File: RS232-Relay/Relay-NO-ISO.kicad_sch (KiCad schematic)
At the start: 7 parts, among them K13 G5V-1, Q13 2N3904

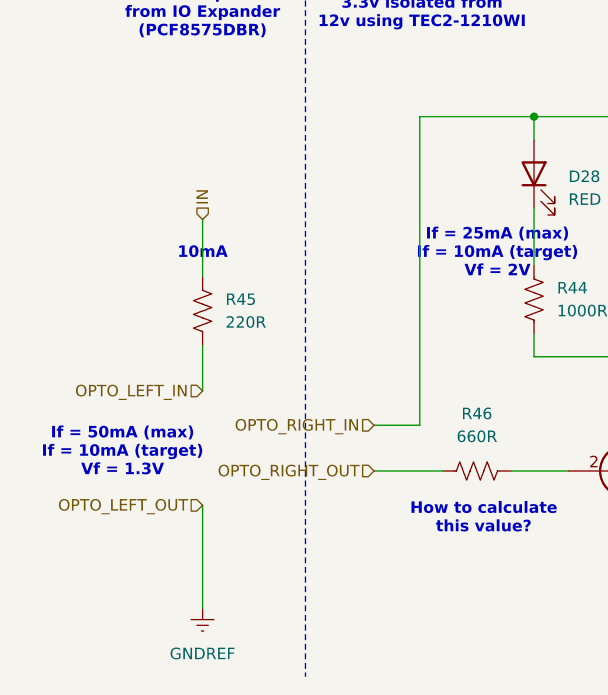
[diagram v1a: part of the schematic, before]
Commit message: Switching to drain rather than source
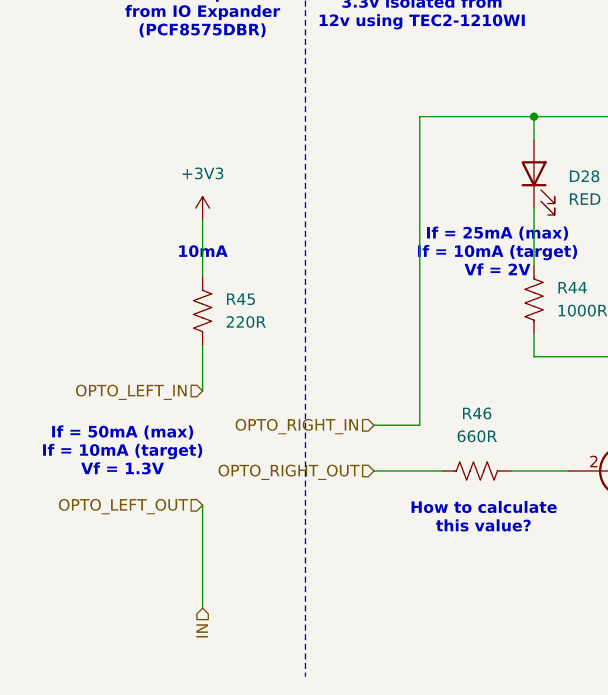
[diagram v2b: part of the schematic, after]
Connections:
- net IN: no longer R45.2
- new net +3V3: R45.2
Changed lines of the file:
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@@
-		)
-	)
-	(hierarchical_label "IN"
-		(shape input)
-		(at 91.44 72.39 90)
-		(fields_autoplaced yes)
-		(effects
-			(font
-				(size 1.27 1.27)
-			)
-			(justify left)
 		)
 	)
@@
 		)
 	)
+	(hierarchical_label "IN"
+		(shape input)
+		(at 91.44 115.57 270)
+		(fields_autoplaced yes)
+		(effects
+			(font
+				(size 1.27 1.27)
+			)
+			(justify right)
+		)
+	)
 	(symbol
-		(lib_id "power:GNDREF")
-		(at 91.44 115.57 0)
+		(lib_id "power:+3V3")
+		(at 91.44 72.39 0)
 		(unit 1)
 		(exclude_from_sim no)
@@
 		(dnp no)
 		(fields_autoplaced yes)
-		(property "Reference" "#PWR069"
-			(at 91.44 121.92 0)
+		(property "Reference" "#PWR052"
+			(at 91.44 76.2 0)
 			(effects
 				(font
@@
 			)
 		)
-		(property "Value" "GNDREF"
-			(at 91.44 120.65 0)
+		(property "Value" "+3V3"
+			(at 91.44 67.31 0)
 			(effects
 				(font
@@
 		)
 		(property "Footprint" ""
-			(at 91.44 115.57 0)
+			(at 91.44 72.39 0)
 			(effects
 				(font
@@
 		)
 		(property "Datasheet" ""
-			(at 91.44 115.57 0)
+			(at 91.44 72.39 0)
 			(effects
 				(font
@@
 			)
 		)
-		(property "Description" "Power symbol creates a global label with name \"GNDREF\" , reference supply ground"
-			(at 91.44 115.57 0)
+		(property "Description" "Power symbol creates a global label with name \"+3V3\""
+			(at 91.44 72.39 0)
 			(effects
 				(font
@@
 		(instances
 			(project "RS232-Relay"
+				(path "/6e416d74-c18a-4d9a-a47c-4314aa8f470f/6243990a-47f3-4383-9005-5094cba86ad2/ed71aacf-ab14-4c62-832c-243c3f9cdc45"
+					(reference "#PWR052")
+					(unit 1)
+				)
 				(path "/6e416d74-c18a-4d9a-a47c-4314aa8f470f/6243990a-47f3-4383-9005-5094cba86ad2/f12f86a4-1d04-4329-8ad3-ff7853ea8b11"
-					(reference "#PWR069")
+					(reference "#PWR02")
 					(unit 1)
 				)
 				(path "/6e416d74-c18a-4d9a-a47c-4314aa8f470f/4cc60208-aa63-44fd-9447-92e9d40fbb60/f12f86a4-1d04-4329-8ad3-ff7853ea8b11"
-					(reference "#PWR072")
+					(reference "#PWR028")
 					(unit 1)
 				)
 				(path "/6e416d74-c18a-4d9a-a47c-4314aa8f470f/f5401bb4-9575-46b7-b322-a153ebcf6229/f12f86a4-1d04-4329-8ad3-ff7853ea8b11"
-					(reference "#PWR075")
+					(reference "#PWR032")
 					(unit 1)
 				)
 				(path "/6e416d74-c18a-4d9a-a47c-4314aa8f470f/6243990a-47f3-4383-9005-5094cba86ad2/64c8bb9c-8205-4bce-bd9e-bf40b585cd58"
-					(reference "#PWR02")
+					(reference "#PWR033")
 					(unit 1)
 				)
 				(path "/6e416d74-c18a-4d9a-a47c-4314aa8f470f/4cc60208-aa63-44fd-9447-92e9d40fbb60/64c8bb9c-8205-4bce-bd9e-bf40b585cd58"
-					(reference "#PWR028")
+					(reference "#PWR037")
 					(unit 1)
 				)
 				(path "/6e416d74-c18a-4d9a-a47c-4314aa8f470f/f5401bb4-9575-46b7-b322-a153ebcf6229/64c8bb9c-8205-4bce-bd9e-bf40b585cd58"
-					(reference "#PWR037")
+					(reference "#PWR040")
 					(unit 1)
 				)
 				(path "/6e416d74-c18a-4d9a-a47c-4314aa8f470f/6243990a-47f3-4383-9005-5094cba86ad2/506e8501-abf2-4f3d-9f17-1e03d7258be7"
-					(reference "#PWR040")
+					(reference "#PWR043")
 					(unit 1)
 				)
 				(path "/6e416d74-c18a-4d9a-a47c-4314aa8f470f/4cc60208-aa63-44fd-9447-92e9d40fbb60/506e8501-abf2-4f3d-9f17-1e03d7258be7"
-					(reference "#PWR043")
+					(reference "#PWR046")
 					(unit 1)
 				)
 				(path "/6e416d74-c18a-4d9a-a47c-4314aa8f470f/f5401bb4-9575-46b7-b322-a153ebcf6229/506e8501-abf2-4f3d-9f17-1e03d7258be7"
-					(reference "#PWR046")
-					(unit 1)
-				)
-				(path "/6e416d74-c18a-4d9a-a47c-4314aa8f470f/6243990a-47f3-4383-9005-5094cba86ad2/ed71aacf-ab14-4c62-832c-243c3f9cdc45"
 					(reference "#PWR049")
 					(unit 1)
 				)
 				(path "/6e416d74-c18a-4d9a-a47c-4314aa8f470f/4cc60208-aa63-44fd-9447-92e9d40fbb60/ed71aacf-ab14-4c62-832c-243c3f9cdc45"
-					(reference "#PWR052")
+					(reference "#PWR055")
 					(unit 1)
 				)
 				(path "/6e416d74-c18a-4d9a-a47c-4314aa8f470f/f5401bb4-9575-46b7-b322-a153ebcf6229/ed71aacf-ab14-4c62-832c-243c3f9cdc45"
-					(reference "#PWR055")
+					(reference "#PWR057")
 					(unit 1)
 				)

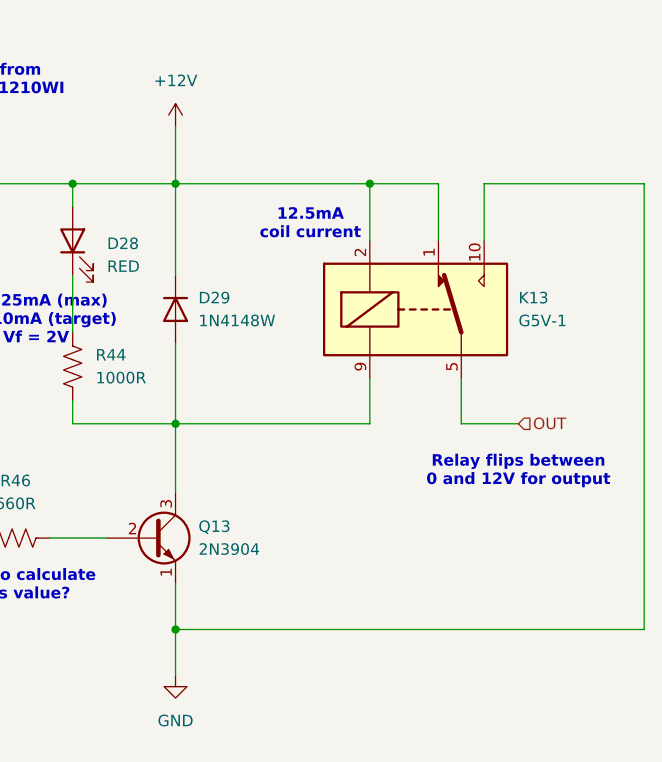
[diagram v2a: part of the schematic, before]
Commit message: Figuring out the relay NC/NO connections
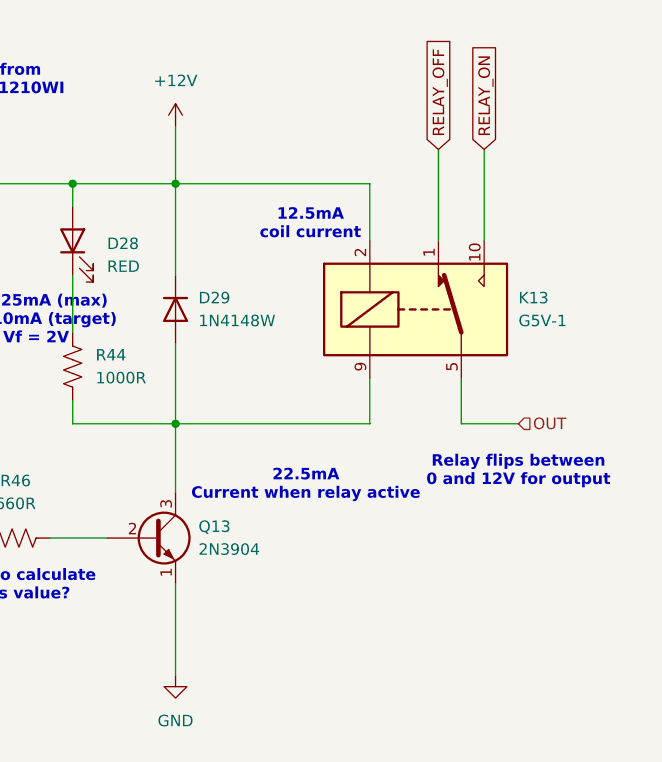
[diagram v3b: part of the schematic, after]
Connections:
- net +12V: no longer K13.1
- net GND: no longer K13.10
- new net RELAY_OFF: K13.1
- new net RELAY_ON: K13.10
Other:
- note added: "22.5mA Current when relay active"
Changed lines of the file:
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@@
 	(paper "A4")
-	(junction
-		(at 161.29 60.96)
-		(diameter 0)
-		(color 0 0 0 0)
-	)
 	(junction
 		(at 139.7 60.96)
@@
 	)
 	(junction
-		(at 139.7 110.49)
-		(diameter 0)
-		(color 0 0 0 0)
-	)
-	(junction
 		(at 139.7 87.63)
 		(diameter 0)
@@
 		)
 	)
-	(wire
-		(pts
-			(xy 173.99 60.96) (xy 191.77 60.96)
-		)
-		(stroke
-			(width 0)
-			(type default)
-		)
-	)
 	(polyline
 		(pts
@@
 	(wire
 		(pts
-			(xy 139.7 110.49) (xy 139.7 115.57)
-		)
-		(stroke
-			(width 0)
-			(type default)
-		)
-	)
-	(wire
-		(pts
 			(xy 139.7 78.74) (xy 139.7 87.63)
 		)
@@
 	(wire
 		(pts
-			(xy 191.77 110.49) (xy 139.7 110.49)
-		)
-		(stroke
-			(width 0)
-			(type default)
-		)
-	)
-	(wire
-		(pts
 			(xy 139.7 87.63) (xy 161.29 87.63)
 		)
@@
 	(wire
 		(pts
-			(xy 173.99 67.31) (xy 173.99 60.96)
+			(xy 173.99 57.15) (xy 173.99 67.31)
 		)
 		(stroke
@@
 	(wire
 		(pts
-			(xy 168.91 60.96) (xy 161.29 60.96)
-		)
-		(stroke
-			(width 0)
-			(type default)
-		)
-	)
-	(wire
-		(pts
-			(xy 191.77 60.96) (xy 191.77 110.49)
-		)
-		(stroke
-			(width 0)
-			(type default)
-		)
-	)
-	(wire
-		(pts
-			(xy 168.91 67.31) (xy 168.91 60.96)
+			(xy 168.91 57.15) (xy 168.91 67.31)
 		)
 		(stroke
@@
 	(wire
 		(pts
-			(xy 139.7 105.41) (xy 139.7 110.49)
+			(xy 139.7 105.41) (xy 139.7 115.57)
 		)
 		(stroke
@@
 		)
 	)
+	(text "22.5mA \nCurrent when relay active"
+		(exclude_from_sim no)
+		(at 154.178 94.488 0)
+		(effects
+			(font
+				(size 1.27 1.27)
+				(thickness 0.254)
+				(bold yes)
+				(color 255 0 0 1)
+			)
+		)
+	)
 	(text "3v3 input\nfrom IO Expander\n(PCF8575DBR)"
 		(exclude_from_sim no)
@@
 			)
 		)
+	)
+	(global_label "RELAY_ON"
+		(shape input)
+		(at 173.99 57.15 90)
+		(fields_autoplaced yes)
+		(effects
+			(font
+				(size 1.27 1.27)
+			)
+			(justify left)
+		)
+		(property "Intersheetrefs" "${INTERSHEET_REFS}"
+			(at 173.99 44.9119 90)
+			(effects
+				(font
+					(size 1.27 1.27)
+				)
+				(justify left)
+				(hide yes)
+			)
+		)
+	)
+	(global_label "RELAY_OFF"
+		(shape input)
+		(at 168.91 57.15 90)
+		(fields_autoplaced yes)
+		(effects
+			(font
+				(size 1.27 1.27)
+			)
+			(justify left)
+		)
+		(property "Intersheetrefs" "${INTERSHEET_REFS}"
+			(at 168.91 44.0652 90)
+			(effects
+				(font
+					(size 1.27 1.27)
+				)
+				(justify left)
+				(hide yes)
+			)
+		)

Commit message: Figured out a solution, now for implementation
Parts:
- added JP1, JP49: Jumper_3_Bridged12, Jumper:SolderJumper-3_P1.3mm_Bridged2Bar12_RoundedPad1.0x1.5mm, symbol Jumper:Jumper_3_Bridged12
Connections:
- net +12V: now also JP1.3 (B), JP49.1 (A)
- net GND: now also JP1.1 (A), JP49.3 (B)
- net RELAY_OFF: now also JP1.2 (C)
- net RELAY_ON: now also JP49.2 (C)

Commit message: Schematic complete
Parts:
- added TP2: Backup, TestPoint:TestPoint_Pad_D1.0mm, symbol Connector:TestPoint
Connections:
- net IN: now also TP2.1
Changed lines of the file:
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@@
+	)
+	(junction
+		(at 91.44 110.49)
+		(diameter 0)
+		(color 0 0 0 0)
 	)
 	(junction
@@
 	(wire
 		(pts
+			(xy 86.36 110.49) (xy 91.44 110.49)
+		)
+		(stroke
+			(width 0)
+			(type default)
+		)
+	)
+	(wire
+		(pts
 			(xy 222.25 62.23) (xy 228.6 62.23)
 		)
@@
 	(wire
 		(pts
+			(xy 91.44 110.49) (xy 91.44 104.14)
+		)
+		(stroke
+			(width 0)
+			(type default)
+		)
+	)
+	(wire
+		(pts
 			(xy 128.27 63.5) (xy 128.27 60.96)
 		)
@@
 	(wire
 		(pts
-			(xy 91.44 115.57) (xy 91.44 104.14)
+			(xy 91.44 115.57) (xy 91.44 110.49)
 		)
 		(stroke
@@
 					(unit 1)
 				)
+			)
+		)
+	)
+	(symbol
+		(lib_id "Connector:TestPoint")
+		(at 86.36 110.49 90)
+		(unit 1)
+		(exclude_from_sim no)
+		(in_bom yes)
+		(on_board yes)
+		(dnp no)
+		(fields_autoplaced yes)
+		(property "Reference" "TP2"
+			(at 83.058 105.41 90)
+			(effects
+				(font
+					(size 1.27 1.27)
+				)
+			)
+		)
+		(property "Value" "Backup"
+			(at 83.058 107.95 90)
+			(effects
+				(font
+					(size 1.27 1.27)
+				)
+			)
+		)
+		(property "Footprint" "TestPoint:TestPoint_Pad_D1.0mm"
+			(at 86.36 105.41 0)
+			(effects
+				(font
+					(size 1.27 1.27)
+				)
+				(hide yes)
+			)
+		)
+		(property "Datasheet" "~"
+			(at 86.36 105.41 0)
+			(effects
+				(font
+					(size 1.27 1.27)
+				)
+				(hide yes)
+			)
+		)
+		(property "Description" "test point"
+			(at 86.36 110.49 0)
+			(effects
+				(font
+					(size 1.27 1.27)
+				)
+				(hide yes)
+			)
+		)
+		(pin "1"
+		)
+		(instances
+			(project "RS232-Relay"
+				(path "/6e416d74-c18a-4d9a-a47c-4314aa8f470f/6243990a-47f3-4383-9005-5094cba86ad2/f12f86a4-1d04-4329-8ad3-ff7853ea8b11"
+					(reference "TP2")
+					(unit 1)
+				)
+				(path "/6e416d74-c18a-4d9a-a47c-4314aa8f470f/4cc60208-aa63-44fd-9447-92e9d40fbb60/f12f86a4-1d04-4329-8ad3-ff7853ea8b11"
+					(reference "TP3")
+					(unit 1)
+				)
+				(path "/6e416d74-c18a-4d9a-a47c-4314aa8f470f/f5401bb4-9575-46b7-b322-a153ebcf6229/f12f86a4-1d04-4329-8ad3-ff7853ea8b11"
+					(reference "TP14")
+					(unit 1)
+				)
+				(path "/6e416d74-c18a-4d9a-a47c-4314aa8f470f/6243990a-47f3-4383-9005-5094cba86ad2/64c8bb9c-8205-4bce-bd9e-bf40b585cd58"
+					(reference "TP15")
+					(unit 1)
+				)
+				(path "/6e416d74-c18a-4d9a-a47c-4314aa8f470f/4cc60208-aa63-44fd-9447-92e9d40fbb60/64c8bb9c-8205-4bce-bd9e-bf40b585cd58"
+					(reference "TP16")
+					(unit 1)
+				)
+				(path "/6e416d74-c18a-4d9a-a47c-4314aa8f470f/f5401bb4-9575-46b7-b322-a153ebcf6229/64c8bb9c-8205-4bce-bd9e-bf40b585cd58"
+					(reference "TP17")
+					(unit 1)
+				)
+				(path "/6e416d74-c18a-4d9a-a47c-4314aa8f470f/6243990a-47f3-4383-9005-5094cba86ad2/506e8501-abf2-4f3d-9f17-1e03d7258be7"
+					(reference "TP18")
+					(unit 1)
+				)
+				(path "/6e416d74-c18a-4d9a-a47c-4314aa8f470f/4cc60208-aa63-44fd-9447-92e9d40fbb60/506e8501-abf2-4f3d-9f17-1e03d7258be7"
+					(reference "TP19")
+					(unit 1)
+				)
+				(path "/6e416d74-c18a-4d9a-a47c-4314aa8f470f/f5401bb4-9575-46b7-b322-a153ebcf6229/506e8501-abf2-4f3d-9f17-1e03d7258be7"
+					(reference "TP20")
+					(unit 1)
+				)
+				(path "/6e416d74-c18a-4d9a-a47c-4314aa8f470f/6243990a-47f3-4383-9005-5094cba86ad2/ed71aacf-ab14-4c62-832c-243c3f9cdc45"
+					(reference "TP21")
+					(unit 1)
+				)
+				(path "/6e416d74-c18a-4d9a-a47c-4314aa8f470f/4cc60208-aa63-44fd-9447-92e9d40fbb60/ed71aacf-ab14-4c62-832c-243c3f9cdc45"
+					(reference "TP22")
+					(unit 1)
+				)
+				(path "/6e416d74-c18a-4d9a-a47c-4314aa8f470f/f5401bb4-9575-46b7-b322-a153ebcf6229/ed71aacf-ab14-4c62-832c-243c3f9cdc45"
+					(reference "TP23")
+					(unit 1)
+				)

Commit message: Production v1
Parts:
- K13: LCSC (none) -> C31113
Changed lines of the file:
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@@
+			)
+		)
+		(property "LCSC" " C31113"
+			(at 166.37 74.93 0)
+			(effects
+				(font
+					(size 1.27 1.27)
+				)
+				(hide yes)
 			)
 		)
